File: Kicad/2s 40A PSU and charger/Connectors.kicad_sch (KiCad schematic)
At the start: 18 parts, among them J1 Keystone 3579, J10 G-Switch-GT-USB-7025, J11 1.27mm 4 pin socket, J2 JST XH-S Balance Plug, J3 Keystone 3579, J4 Keystone 3569, J5 Keystone 3569, J6 Keystone 3579, J7 Keystone 3579, J8 Keystone 3569, J9 Keystone 3569

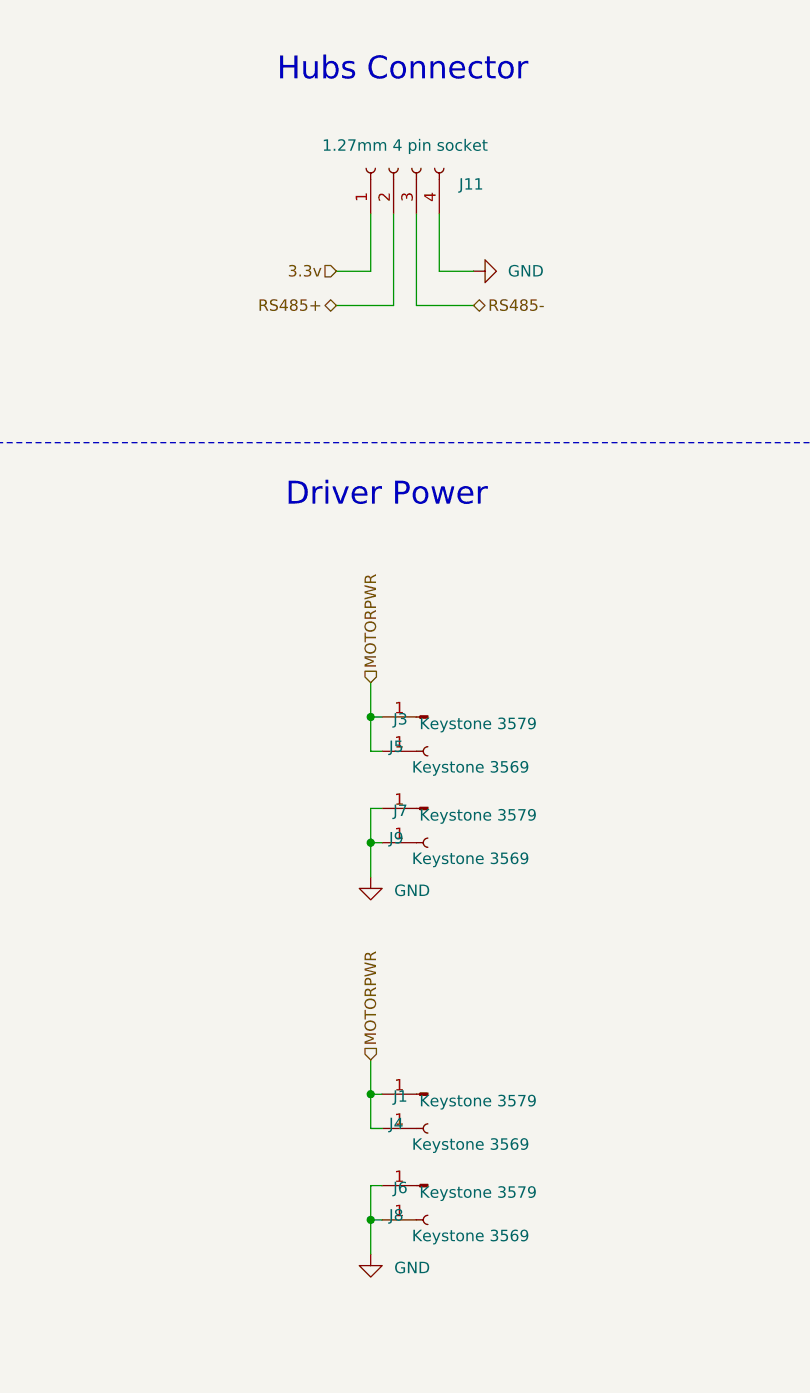
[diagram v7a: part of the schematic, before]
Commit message: Fixed incorrect mosfet pin assignments
This was an issue from the last test board I designed that I didn't catch. The mosfets have different pin assignments for drain, gate, and source, and I had messed those up in the schematic by choosing the wrong symbol. This should be fixed now
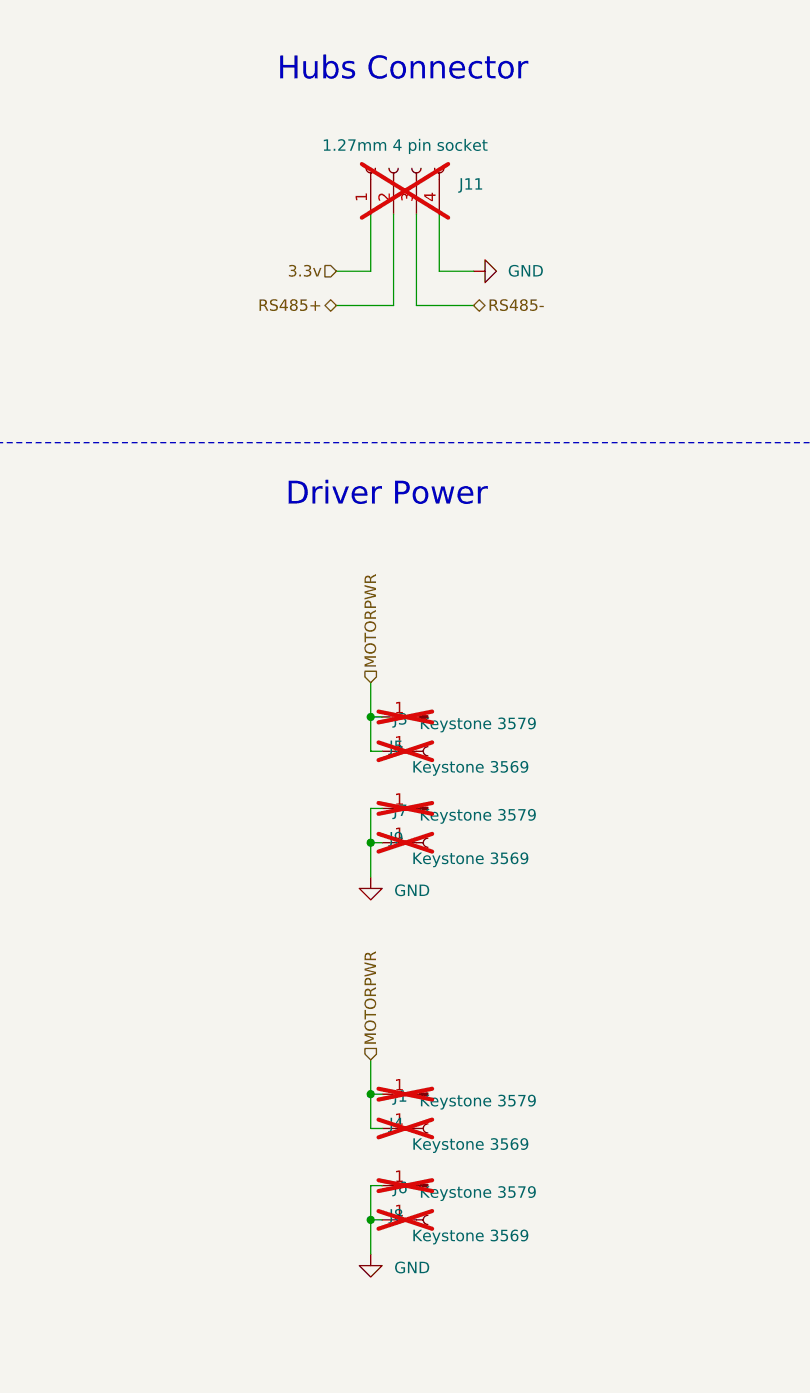
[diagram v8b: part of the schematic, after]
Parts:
- J1, J11, J3, J4, J5, J6, J7, J8, J9: now not fitted
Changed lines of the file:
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@@
 		(in_bom yes)
 		(on_board yes)
-		(dnp no)
+		(dnp yes)
 		(property "Reference" "J4"
 			(at 203.962 140.462 0)
@@
 		(in_bom yes)
 		(on_board yes)
-		(dnp no)
+		(dnp yes)
 		(property "Reference" "J7"
 			(at 205.232 105.664 0)
@@
 		(in_bom yes)
 		(on_board yes)
-		(dnp no)
+		(dnp yes)
 		(property "Reference" "J3"
 			(at 205.232 95.504 0)
@@
 		(in_bom yes)
 		(on_board yes)
-		(dnp no)
+		(dnp yes)
 		(property "Reference" "J1"
 			(at 205.232 137.414 0)
@@
 		(in_bom yes)
 		(on_board yes)
-		(dnp no)
+		(dnp yes)
 		(property "Reference" "J8"
 			(at 203.962 150.622 0)
@@
 		(in_bom yes)
 		(on_board yes)
-		(dnp no)
+		(dnp yes)
 		(property "Reference" "J5"
 			(at 203.962 98.552 0)
@@
 		(in_bom yes)
 		(on_board yes)
-		(dnp no)
+		(dnp yes)
 		(property "Reference" "J9"
 			(at 203.962 108.712 0)
@@
 		(in_bom yes)
 		(on_board yes)
-		(dnp no)
+		(dnp yes)
 		(property "Reference" "J6"
 			(at 205.232 147.574 0)
@@
 		(in_bom yes)
 		(on_board yes)
-		(dnp no)
+		(dnp yes)
 		(property "Reference" "J11"
 			(at 213.106 36.068 90)
